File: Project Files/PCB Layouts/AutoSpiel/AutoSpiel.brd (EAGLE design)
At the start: 140.9 x 100 mm, 10 parts, among them Q1 TIP120

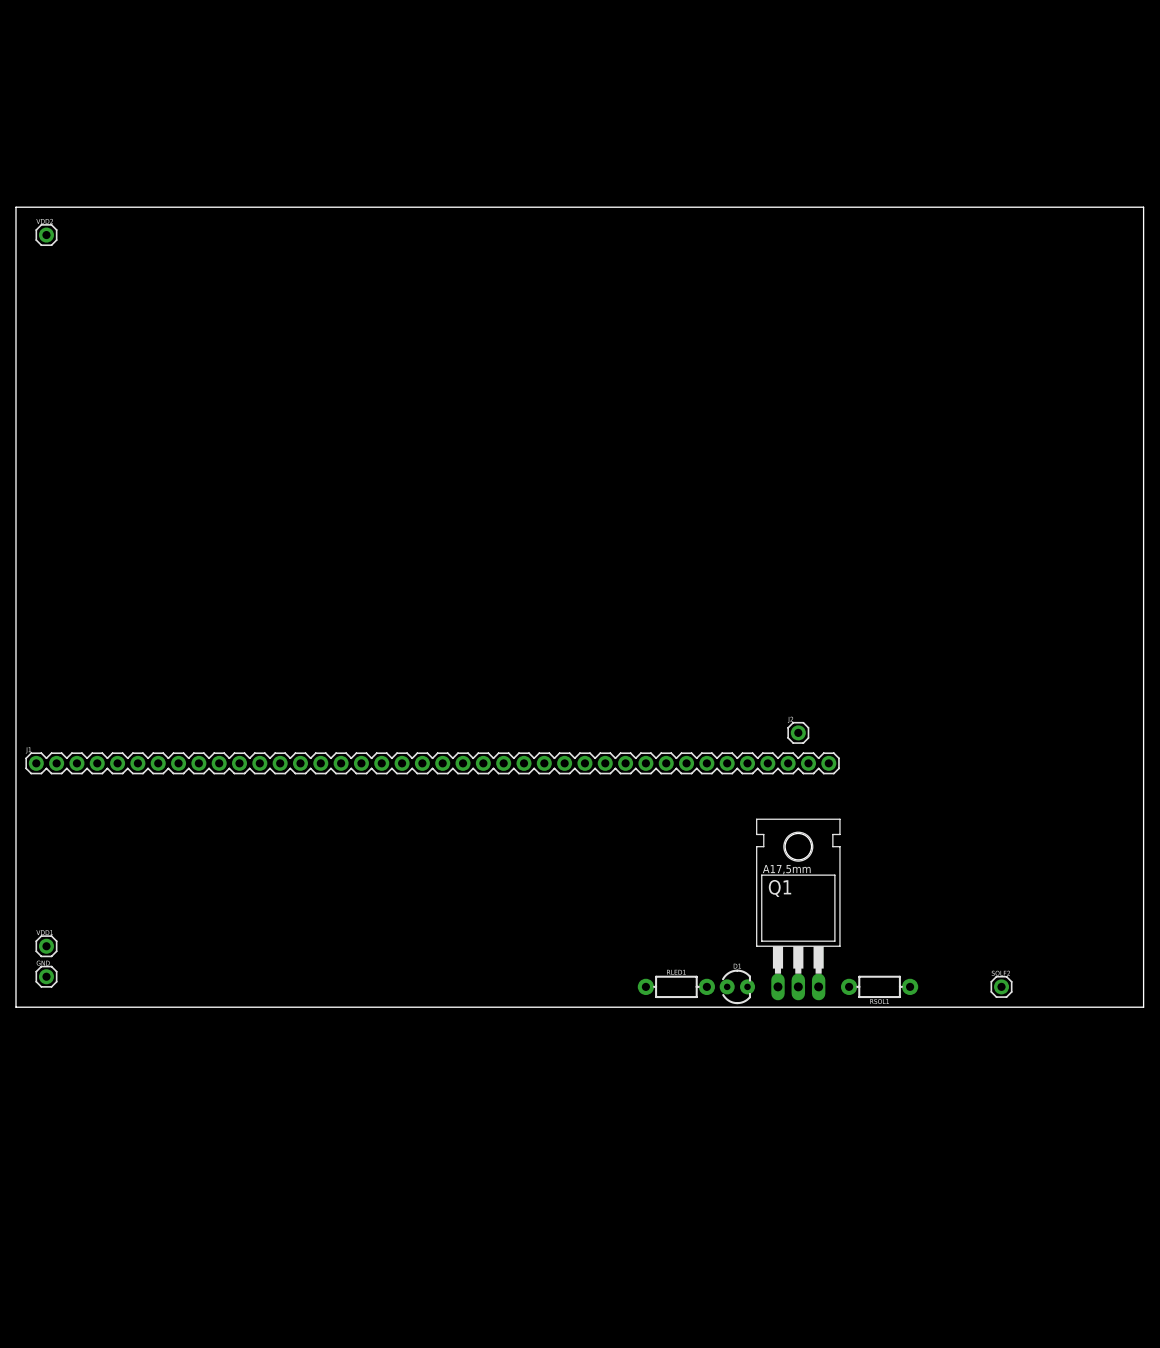
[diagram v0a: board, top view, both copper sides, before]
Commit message: Added more to the board to do fit testing
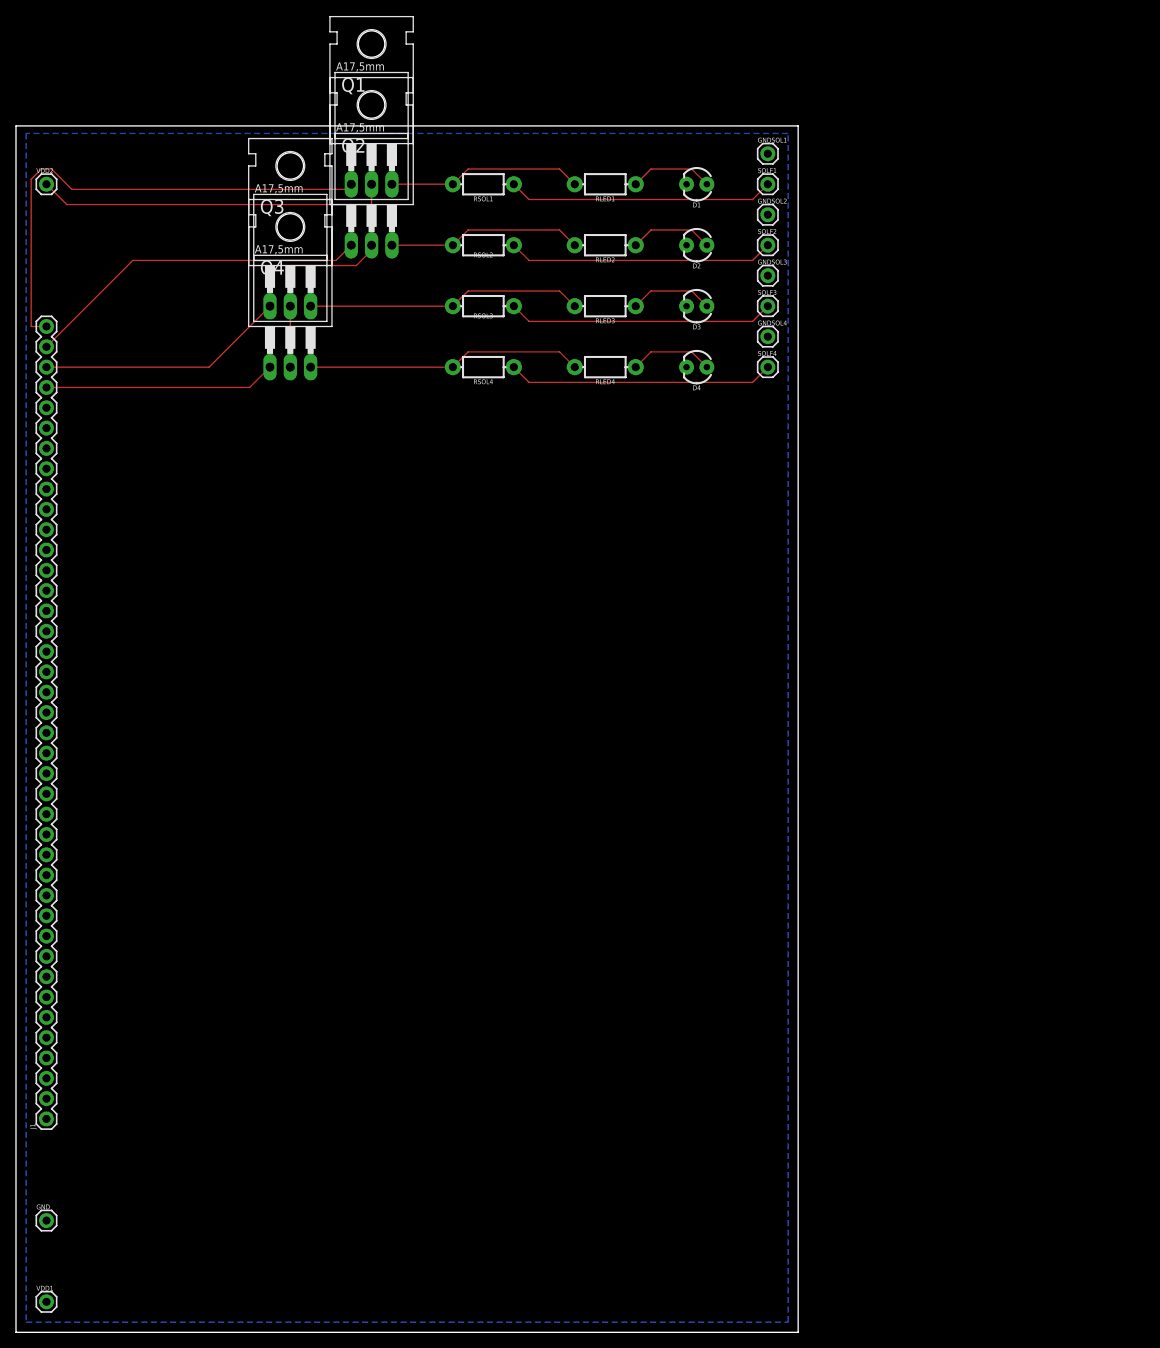
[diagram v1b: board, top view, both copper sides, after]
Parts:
- removed J2: (no value), SparkFun-Connectors:1X01
- added D2, D3, D4: (no value), SparkFun-LED:LED_3MM
- added GNDSOL1, GNDSOL2, GNDSOL3, GNDSOL4, SOLF1, SOLF3, SOLF4: (no value), SparkFun-Connectors:1X01
- added Q2, Q3, Q4: TIP120, transistor-power:TO220AH
- added RLED2, RLED3, RLED4, RSOL2, RSOL3, RSOL4: 10k, SparkFun-Resistors:AXIAL-0.3-KIT
- moved Q1 113.6 mm to (-72.4, 109.2)
- moved RSOL1 111.9 mm to (-58.4, 102.9)
- moved RLED1 100.7 mm to (-43.2, 102.9), turned to 180 degrees
- moved D1 100.5 mm to (-31.8, 102.9), turned to 180 degrees
- moved SOLF2 97.2 mm to (-22.9, 95.2)
- moved J1 44.5 mm to (-113.0, -14.0), turned to 90 degrees
- moved VDD1 44.4 mm to (-113.0, -36.8)
- moved GND 30.5 mm to (-113.0, -26.7)
- moved VDD2 6.35 mm to (-113.0, 102.9)
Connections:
- new net N$1: Q2.E, RLED2.P$2, RSOL2.P$2
- new net N$10: D4.A, RLED4.P$1
- new net N$2: RSOL2.P$1, SOLF2.1
- new net N$3: D2.A, RLED2.P$1
- new net N$4: Q3.E, RLED3.P$2, RSOL3.P$2
- new net N$5: RSOL3.P$1, SOLF3.1
- new net N$7: D3.A, RLED3.P$1
- new net N$8: Q4.E, RLED4.P$2, RSOL4.P$2
- new net N$9: RSOL4.P$1, SOLF4.1
- net F#2: now also Q2.B
- net G#2: now also Q4.B
- net G2: now also Q3.B
- net GND: now also D2.K, D3.K, D4.K, GNDSOL1.1, GNDSOL2.1, GNDSOL3.1, GNDSOL4.1; no longer J2.1
- net N$37: now also SOLF1.1; no longer SOLF2.1
- net VDD2: now also Q2.C, Q3.C, Q4.C
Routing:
- net VDD2: track 0.00 -> 73.6 mm
- net F2: track 0.00 -> 62.2 mm
- net F#2: track 0.00 -> 43.4 mm
- net N$8: track 0.00 -> 34.6 mm
- net N$4: track 0.00 -> 34.6 mm
- net N$9: track 0.00 -> 33.3 mm
- net N$5: track 0.00 -> 33.3 mm
- net N$37: track 0.00 -> 33.3 mm
- net N$2: track 0.00 -> 33.3 mm
- net G2: track 0.00 -> 31.1 mm
- net G#2: track 0.00 -> 29.0 mm
- net N$6: track 0.00 -> 24.4 mm
- net N$1: track 0.00 -> 24.4 mm
- net N$7: track 0.00 -> 10.5 mm
- net N$38: track 0.00 -> 10.5 mm
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- added copper zone on layer 16, net GND
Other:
- board size 140.9 x 100 mm -> 97.8 x 150.8 mm
